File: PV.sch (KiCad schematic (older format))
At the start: 30 parts

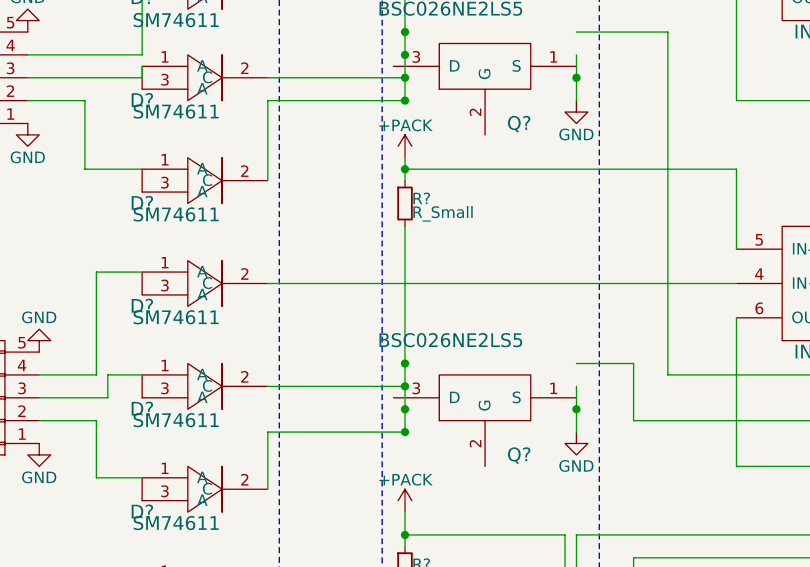
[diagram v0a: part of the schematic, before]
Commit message: (Confirmation) BPack Ammeter + Proctection Circuit Edit
Making sure the last commit pushed all edits.
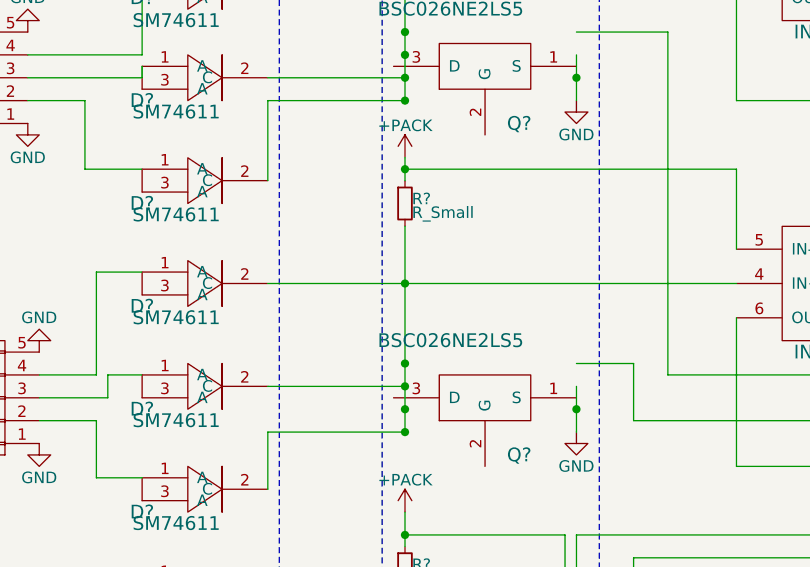
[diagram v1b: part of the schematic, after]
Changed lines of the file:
@@
 Text Notes 2300 300  0    60   ~ 0
 Might have to move current sensor to other side of mosfet
+Connection ~ 3800 2450
 $EndSCHEMATC

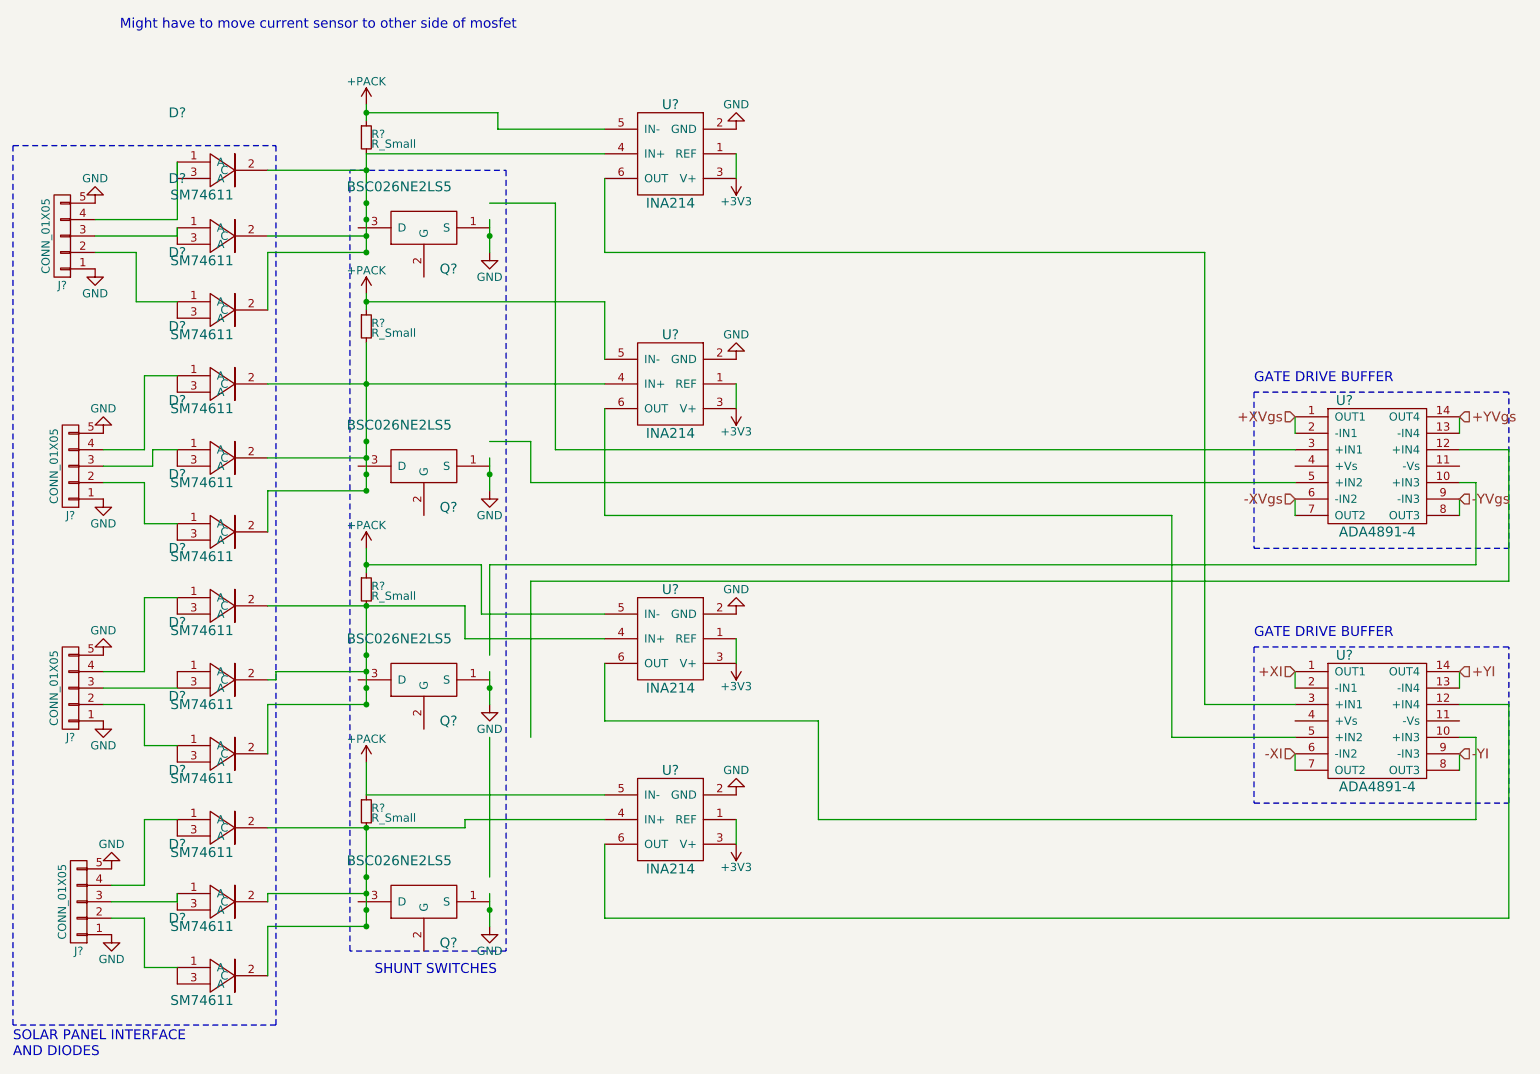
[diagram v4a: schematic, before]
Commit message: Created netlist
Still missing deployment and RBL switches
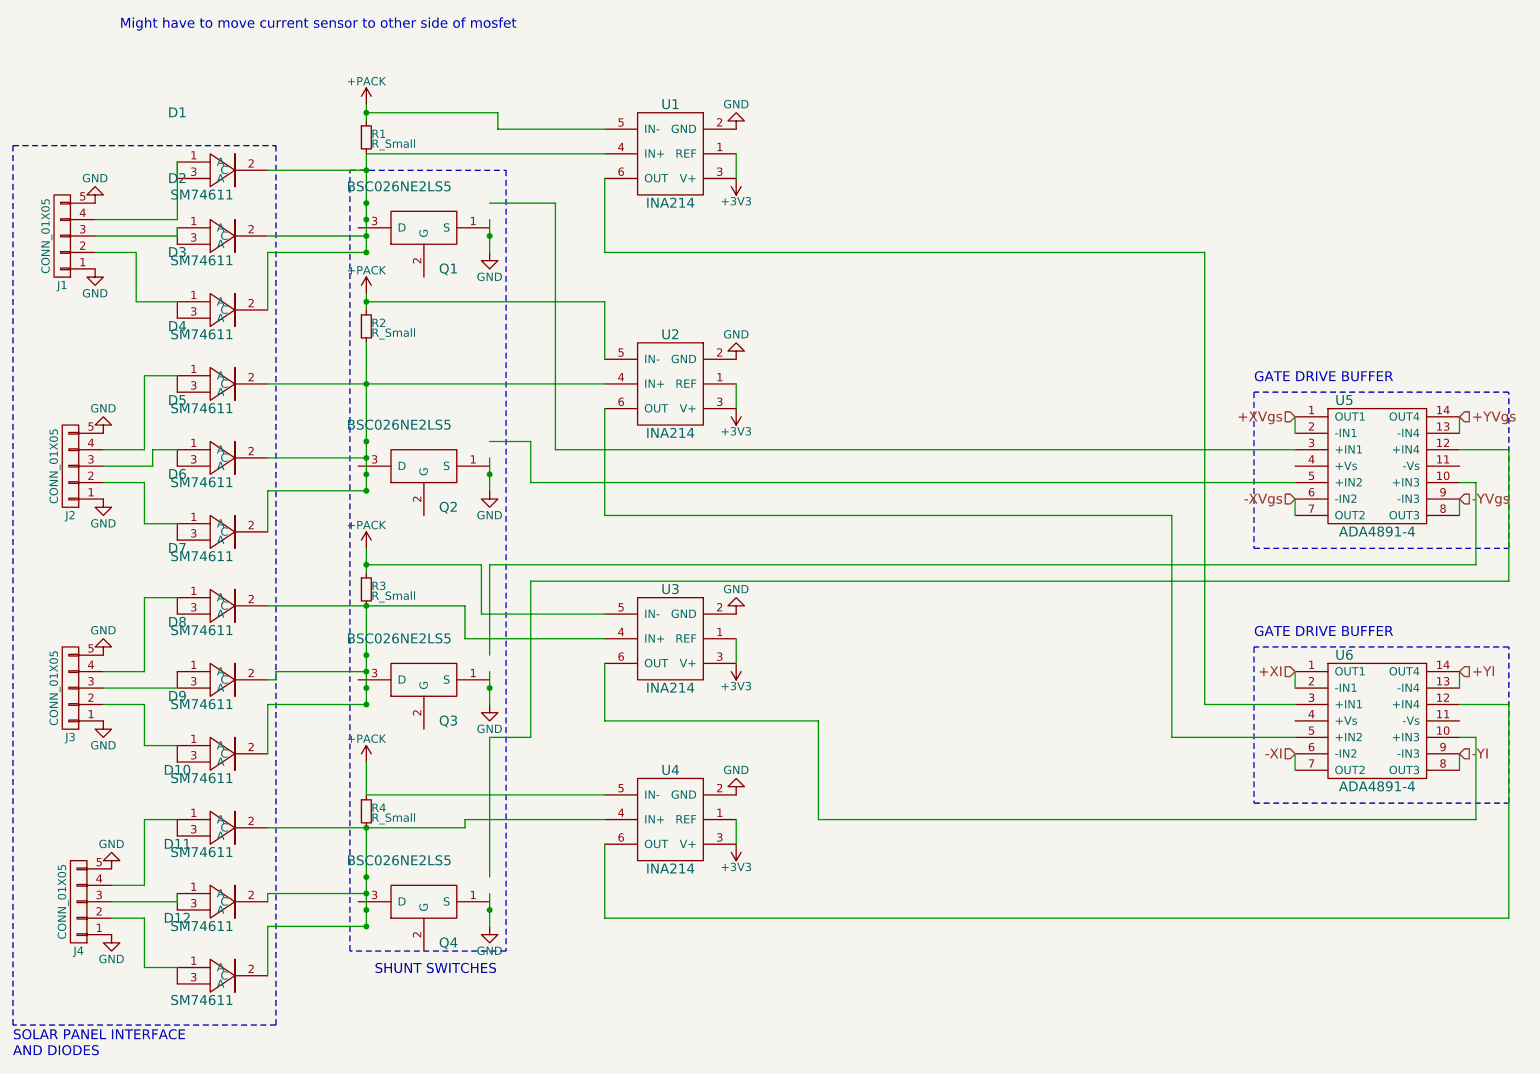
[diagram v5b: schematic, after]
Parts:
- gave numbers to parts that had none: 30
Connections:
- wire segments 121 -> 122

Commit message: Began interfacing with µC
Also all 9V should now be 5V, change resistors accordingly.
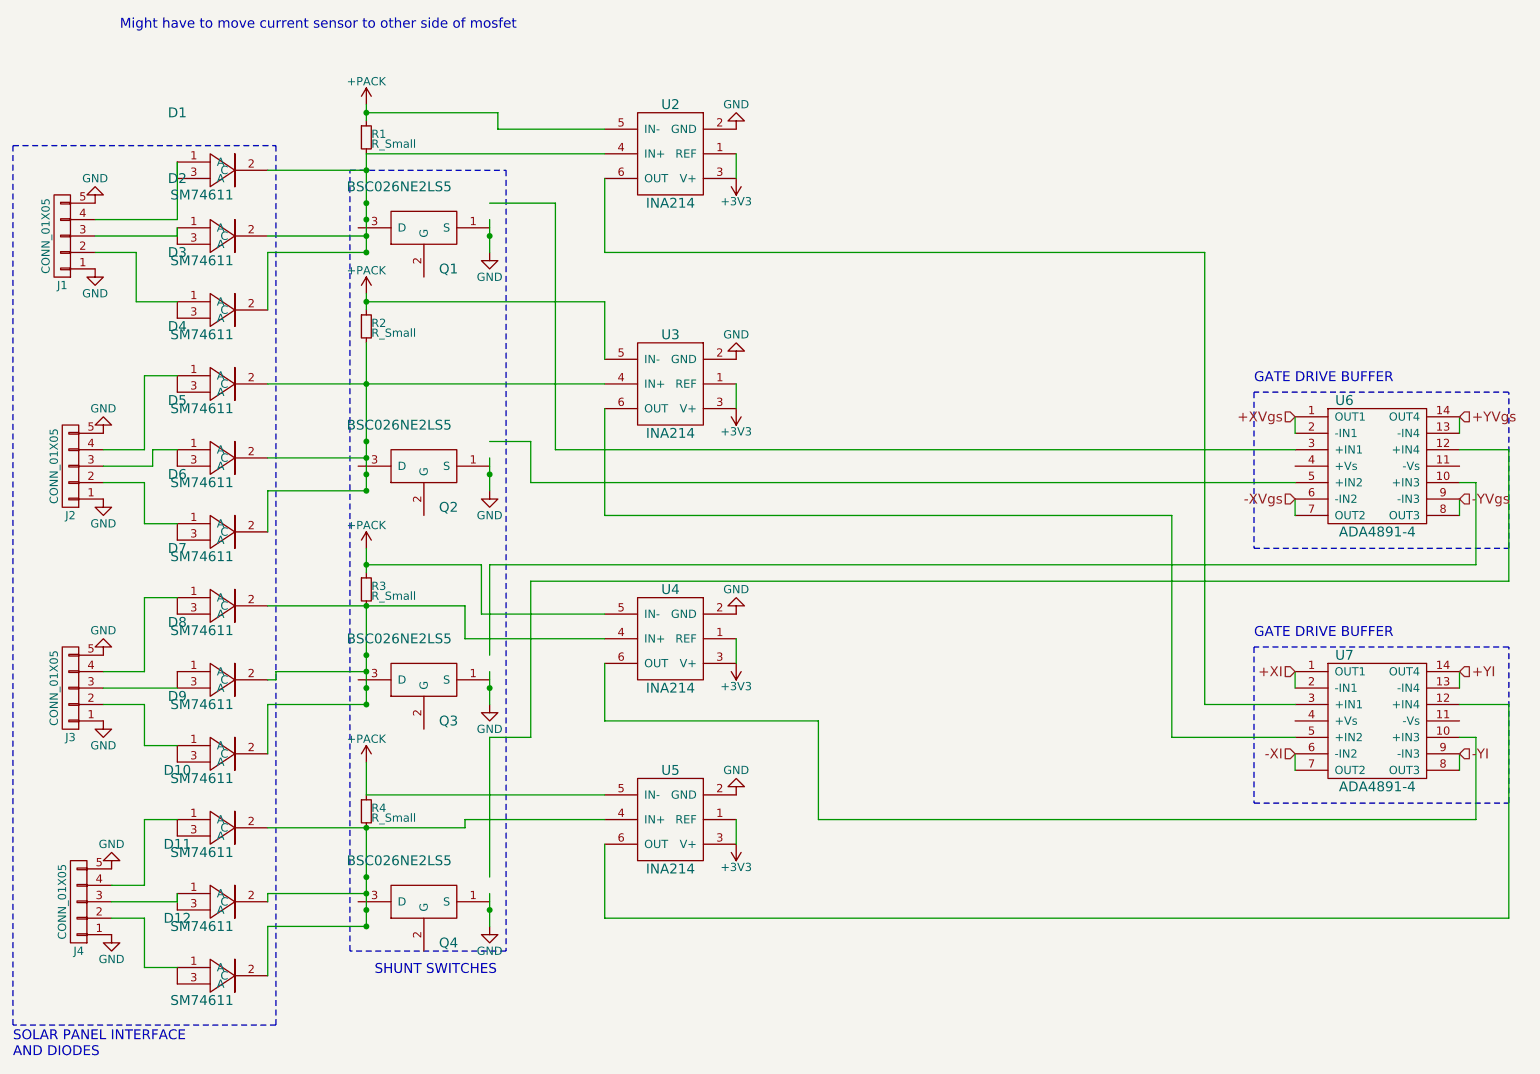
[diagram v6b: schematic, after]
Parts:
- renumbered U1 to U2, U2 to U3, U3 to U4, U4 to U5, U5 to U6, U6 to U7
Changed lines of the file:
@@
 LIBS:ina214
 LIBS:tps61088
+LIBS:cdh_lib
 LIBS:eps_v1-cache
 EELAYER 25 0
@@
 $EndComp
 $Comp
-L GND #PWR016
+L GND #PWR23
 U 1 1 59E8CF5B
 P 2250 5800
-F 0 "#PWR016" H 2250 5550 50  0001 C CNN
+F 0 "#PWR23" H 2250 5550 50  0001 C CNN
 F 1 "GND" H 2250 5650 50  0000 C CNN
 F 2 "" H 2250 5800 50  0001 C CNN
@@
 $EndComp
 $Comp
-L GND #PWR017
+L GND #PWR22
 U 1 1 59E8CF61
 P 2250 5400
-F 0 "#PWR017" H 2250 5150 50  0001 C CNN
+F 0 "#PWR22" H 2250 5150 50  0001 C CNN
 F 1 "GND" H 2250 5250 50  0000 C CNN
 F 2 "" H 2250 5400 50  0001 C CNN
@@
 $EndComp
 $Comp
-L GND #PWR018
+L GND #PWR21
 U 1 1 59E8CF67
 P 2200 4500
-F 0 "#PWR018" H 2200 4250 50  0001 C CNN
+F 0 "#PWR21" H 2200 4250 50  0001 C CNN
 F 1 "GND" H 2200 4350 50  0000 C CNN
 F 2 "" H 2200 4500 50  0001 C CNN
@@
 $EndComp
 $Comp
-L GND #PWR019
+L GND #PWR20
 U 1 1 59E8CF6D
 P 2200 4100
-F 0 "#PWR019" H 2200 3850 50  0001 C CNN
+F 0 "#PWR20" H 2200 3850 50  0001 C CNN
 F 1 "GND" H 2200 3950 50  0000 C CNN
 F 2 "" H 2200 4100 50  0001 C CNN
@@
 $EndComp
 $Comp
-L GND #PWR020
+L GND #PWR18
 U 1 1 59E8CF73
 P 2200 2750
-F 0 "#PWR020" H 2200 2500 50  0001 C CNN
+F 0 "#PWR18" H 2200 2500 50  0001 C CNN
 F 1 "GND" H 2200 2600 50  0000 C CNN
 F 2 "" H 2200 2750 50  0001 C CNN
@@
 $EndComp
 $Comp
-L GND #PWR021
+L GND #PWR16
 U 1 1 59E8CF79
 P 2150 1350
-F 0 "#PWR021" H 2150 1100 50  0001 C CNN
+F 0 "#PWR16" H 2150 1100 50  0001 C CNN
 F 1 "GND" H 2150 1200 50  0000 C CNN
 F 2 "" H 2150 1350 50  0001 C CNN
@@
 $EndComp
 $Comp
-L GND #PWR022
+L GND #PWR19
 U 1 1 59E8CF7F
 P 2200 3150
-F 0 "#PWR022" H 2200 2900 50  0001 C CNN
+F 0 "#PWR19" H 2200 2900 50  0001 C CNN
 F 1 "GND" H 2200 3000 50  0000 C CNN
 F 2 "" H 2200 3150 50  0001 C CNN
@@
 $EndComp
 $Comp
-L GND #PWR023
+L GND #PWR17
 U 1 1 59E8CF85
 P 2150 1750
-F 0 "#PWR023" H 2150 1500 50  0001 C CNN
+F 0 "#PWR17" H 2150 1500 50  0001 C CNN
 F 1 "GND" H 2150 1600 50  0000 C CNN
 F 2 "" H 2150 1750 50  0001 C CNN
@@
 SHUNT SWITCHES
 $Comp
-L GND #PWR024
+L GND #PWR29
 U 1 1 59E8CF8D
 P 4550 3100
-F 0 "#PWR024" H 4550 2850 50  0001 C CNN
+F 0 "#PWR29" H 4550 2850 50  0001 C CNN
 F 1 "GND" H 4550 2950 50  0000 C CNN
 F 2 "" H 4550 3100 50  0001 C CNN
@@
 $EndComp
 $Comp
-L GND #PWR025
+L GND #PWR28
 U 1 1 59E8CF93
 P 4550 1650
-F 0 "#PWR025" H 4550 1400 50  0001 C CNN
+F 0 "#PWR28" H 4550 1400 50  0001 C CNN
 F 1 "GND" H 4550 1500 50  0000 C CNN
 F 2 "" H 4550 1650 50  0001 C CNN
@@
 $EndComp
 $Comp
-L GND #PWR026
+L GND #PWR30
 U 1 1 59E8CF99
 P 4550 4400
-F 0 "#PWR026" H 4550 4150 50  0001 C CNN
+F 0 "#PWR30" H 4550 4150 50  0001 C CNN
 F 1 "GND" H 4550 4250 50  0000 C CNN
 F 2 "" H 4550 4400 50  0001 C CNN
@@
 $EndComp
 $Comp
-L GND #PWR027
+L GND #PWR31
 U 1 1 59E8CF9F
 P 4550 5750
-F 0 "#PWR027" H 4550 5500 50  0001 C CNN
+F 0 "#PWR31" H 4550 5500 50  0001 C CNN
 F 1 "GND" H 4550 5600 50  0000 C CNN
 F 2 "" H 4550 5750 50  0001 C CNN
@@
 $EndComp
 $Comp
-L +PACK #PWR028
+L +PACK #PWR27
 U 1 1 59E8CFA5
 P 3800 4750
-F 0 "#PWR028" H 3800 4600 50  0001 C CNN
+F 0 "#PWR27" H 3800 4600 50  0001 C CNN
 F 1 "+PACK" H 3800 4890 50  0000 C CNN
 F 2 "" H 3800 4750 50  0001 C CNN
@@
 $EndComp
 $Comp
-L +PACK #PWR029
+L +PACK #PWR26
 U 1 1 59E8CFAB
 P 3800 3450
-F 0 "#PWR029" H 3800 3300 50  0001 C CNN
+F 0 "#PWR26" H 3800 3300 50  0001 C CNN
 F 1 "+PACK" H 3800 3590 50  0000 C CNN
 F 2 "" H 3800 3450 50  0001 C CNN
@@
 $EndComp
 $Comp
-L +PACK #PWR030
+L +PACK #PWR25
 U 1 1 59E8CFB1
 P 3800 1900
-F 0 "#PWR030" H 3800 1750 50  0001 C CNN
+F 0 "#PWR25" H 3800 1750 50  0001 C CNN
 F 1 "+PACK" H 3800 2040 50  0000 C CNN
 F 2 "" H 3800 1900 50  0001 C CNN
@@
 $EndComp
 $Comp
-L +PACK #PWR031
+L +PACK #PWR24
 U 1 1 59E8CFB7
 P 3800 750
-F 0 "#PWR031" H 3800 600 50  0001 C CNN
+F 0 "#PWR24" H 3800 600 50  0001 C CNN
 F 1 "+PACK" H 3800 890 50  0000 C CNN
 F 2 "" H 3800 750 50  0001 C CNN
@@
 $EndComp
 $Comp
-L ADA4891-4 U5
+L ADA4891-4 U6
 U 1 1 59E8D25C
 P 9950 2950
-F 0 "U5" H 9750 3350 60  0000 C CNN
+F 0 "U6" H 9750 3350 60  0000 C CNN
 F 1 "ADA4891-4" H 9950 2550 60  0000 C CNN
 F 2 "" H 10150 2900 60  0001 C CNN
@@
 -YVgs
 $Comp
-L INA214 U2
+L INA214 U3
 U 1 1 59E90474
 P 5650 2450
-F 0 "U2" H 5650 2150 60  0000 C CNN
+F 0 "U3" H 5650 2150 60  0000 C CNN
 F 1 "INA214" H 5650 2750 60  0000 C CNN
 F 2 "" H 5650 2750 60  0001 C CNN
@@
 $EndComp
 $Comp
-L +3V3 #PWR032
+L +3V3 #PWR35
 U 1 1 59E90639
 P 6050 2600
-F 0 "#PWR032" H 6050 2450 50  0001 C CNN
+F 0 "#PWR35" H 6050 2450 50  0001 C CNN
 F 1 "+3V3" H 6050 2740 50  0000 C CNN
 F 2 "" H 6050 2600 50  0001 C CNN
@@
 $EndComp
 $Comp
-L GND #PWR033
+L GND #PWR34
 U 1 1 59E90719
 P 6050 2300
-F 0 "#PWR033" H 6050 2050 50  0001 C CNN
+F 0 "#PWR34" H 6050 2050 50  0001 C CNN
 F 1 "GND" H 6050 2150 50  0000 C CNN
 F 2 "" H 6050 2300 50  0001 C CNN
@@
 $EndComp
 $Comp
-L INA214 U1
+L INA214 U2
 U 1 1 59E92653
 P 5650 1050
-F 0 "U1" H 5650 750 60  0000 C CNN
+F 0 "U2" H 5650 750 60  0000 C CNN
 F 1 "INA214" H 5650 1350 60  0000 C CNN
 F 2 "" H 5650 1350 60  0001 C CNN
@@
 $EndComp
 $Comp
-L +3V3 #PWR034
+L +3V3 #PWR33
 U 1 1 59E9265A
 P 6050 1200
-F 0 "#PWR034" H 6050 1050 50  0001 C CNN
+F 0 "#PWR33" H 6050 1050 50  0001 C CNN
 F 1 "+3V3" H 6050 1340 50  0000 C CNN
 F 2 "" H 6050 1200 50  0001 C CNN
@@
 $EndComp
 $Comp
-L GND #PWR035
+L GND #PWR32
 U 1 1 59E92660
 P 6050 900
-F 0 "#PWR035" H 6050 650 50  0001 C CNN
+F 0 "#PWR32" H 6050 650 50  0001 C CNN
 F 1 "GND" H 6050 750 50  0000 C CNN
 F 2 "" H 6050 900 50  0001 C CNN
@@
 $EndComp
 $Comp
-L INA214 U3
+L INA214 U4
 U 1 1 59E93A4A
 P 5650 4000
-F 0 "U3" H 5650 3700 60  0000 C CNN
+F 0 "U4" H 5650 3700 60  0000 C CNN
 F 1 "INA214" H 5650 4300 60  0000 C CNN
 F 2 "" H 5650 4300 60  0001 C CNN
@@
 $EndComp
 $Comp
-L +3V3 #PWR036
+L +3V3 #PWR37
 U 1 1 59E93A51
 P 6050 4150
-F 0 "#PWR036" H 6050 4000 50  0001 C CNN
+F 0 "#PWR37" H 6050 4000 50  0001 C CNN
 F 1 "+3V3" H 6050 4290 50  0000 C CNN
 F 2 "" H 6050 4150 50  0001 C CNN
@@
 $EndComp
 $Comp
-L GND #PWR037
+L GND #PWR36
 U 1 1 59E93A57
 P 6050 3850
-F 0 "#PWR037" H 6050 3600 50  0001 C CNN
+F 0 "#PWR36" H 6050 3600 50  0001 C CNN
 F 1 "GND" H 6050 3700 50  0000 C CNN
 F 2 "" H 6050 3850 50  0001 C CNN
@@
 Connection ~ 3800 3800
 $Comp
-L INA214 U4
+L INA214 U5
 U 1 1 59E940A3
 P 5650 5100
-F 0 "U4" H 5650 4800 60  0000 C CNN
+F 0 "U5" H 5650 4800 60  0000 C CNN
 F 1 "INA214" H 5650 5400 60  0000 C CNN
 F 2 "" H 5650 5400 60  0001 C CNN
@@
 $EndComp
 $Comp
-L +3V3 #PWR038
+L +3V3 #PWR39
 U 1 1 59E940AA
 P 6050 5250
-F 0 "#PWR038" H 6050 5100 50  0001 C CNN
+F 0 "#PWR39" H 6050 5100 50  0001 C CNN
 F 1 "+3V3" H 6050 5390 50  0000 C CNN
 F 2 "" H 6050 5250 50  0001 C CNN
@@
 	6050 5100 6050 5250
 $Comp
-L GND #PWR039
+L GND #PWR38
 U 1 1 59E940EB
 P 6050 4950
-F 0 "#PWR039" H 6050 4700 50  0001 C CNN
+F 0 "#PWR38" H 6050 4700 50  0001 C CNN
 F 1 "GND" H 6050 4800 50  0000 C CNN
 F 2 "" H 6050 4950 50  0001 C CNN
@@
 Connection ~ 3800 5150
 $Comp
-L ADA4891-4 U6
+L ADA4891-4 U7
 U 1 1 59E95BC2
 P 9950 4500
-F 0 "U6" H 9750 4900 60  0000 C CNN
+F 0 "U7" H 9750 4900 60  0000 C CNN
 F 1 "ADA4891-4" H 9950 4100 60  0000 C CNN
 F 2 "" H 10150 4450 60  0001 C CNN

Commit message: PCB layout as of 2018-02-07
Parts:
- D1, D10, D11, D12, D2, D3, D4, D5, D6, D7, D8, D9: footprint (none) -> Diodes_SMD:DD-PAK_TO263_SingleDiode
- Q1, Q2, Q3, Q4: footprint (none) -> Housings_SON:VSONP-8-1EP_5x6_Pitch1.27mm
- R1, R2, R3, R4: value R_Small -> 10mΩ; footprint (none) -> Resistors_SMD:R_0603_HandSoldering
- U2, U3, U4, U5: footprint (none) -> kicad-libraries:SC70-6
- U6, U7: footprint (none) -> SMD_Packages:SSOP-14

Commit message: PCB layout as of 2018-02-12
All that’s left to do is add deployment switches
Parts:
- J1, J2, J3, J4: footprint (none) -> Connectors_Hirose:Hirose_DF13-05P-1.25DS_05x1.25mm_Angled
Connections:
- net labels added: +5V
- wire segments 122 -> 114
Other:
- moved on the sheet: Q1, Q2, Q3, Q4
